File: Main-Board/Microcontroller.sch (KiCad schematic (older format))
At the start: 32 parts, among them J6 USB_B_Micro, J7 ICSP, SW1 Reset, U3 FT232RL, U4 ATmega328P-AU, U5 LM1117-5.0, Y1 16 MHz

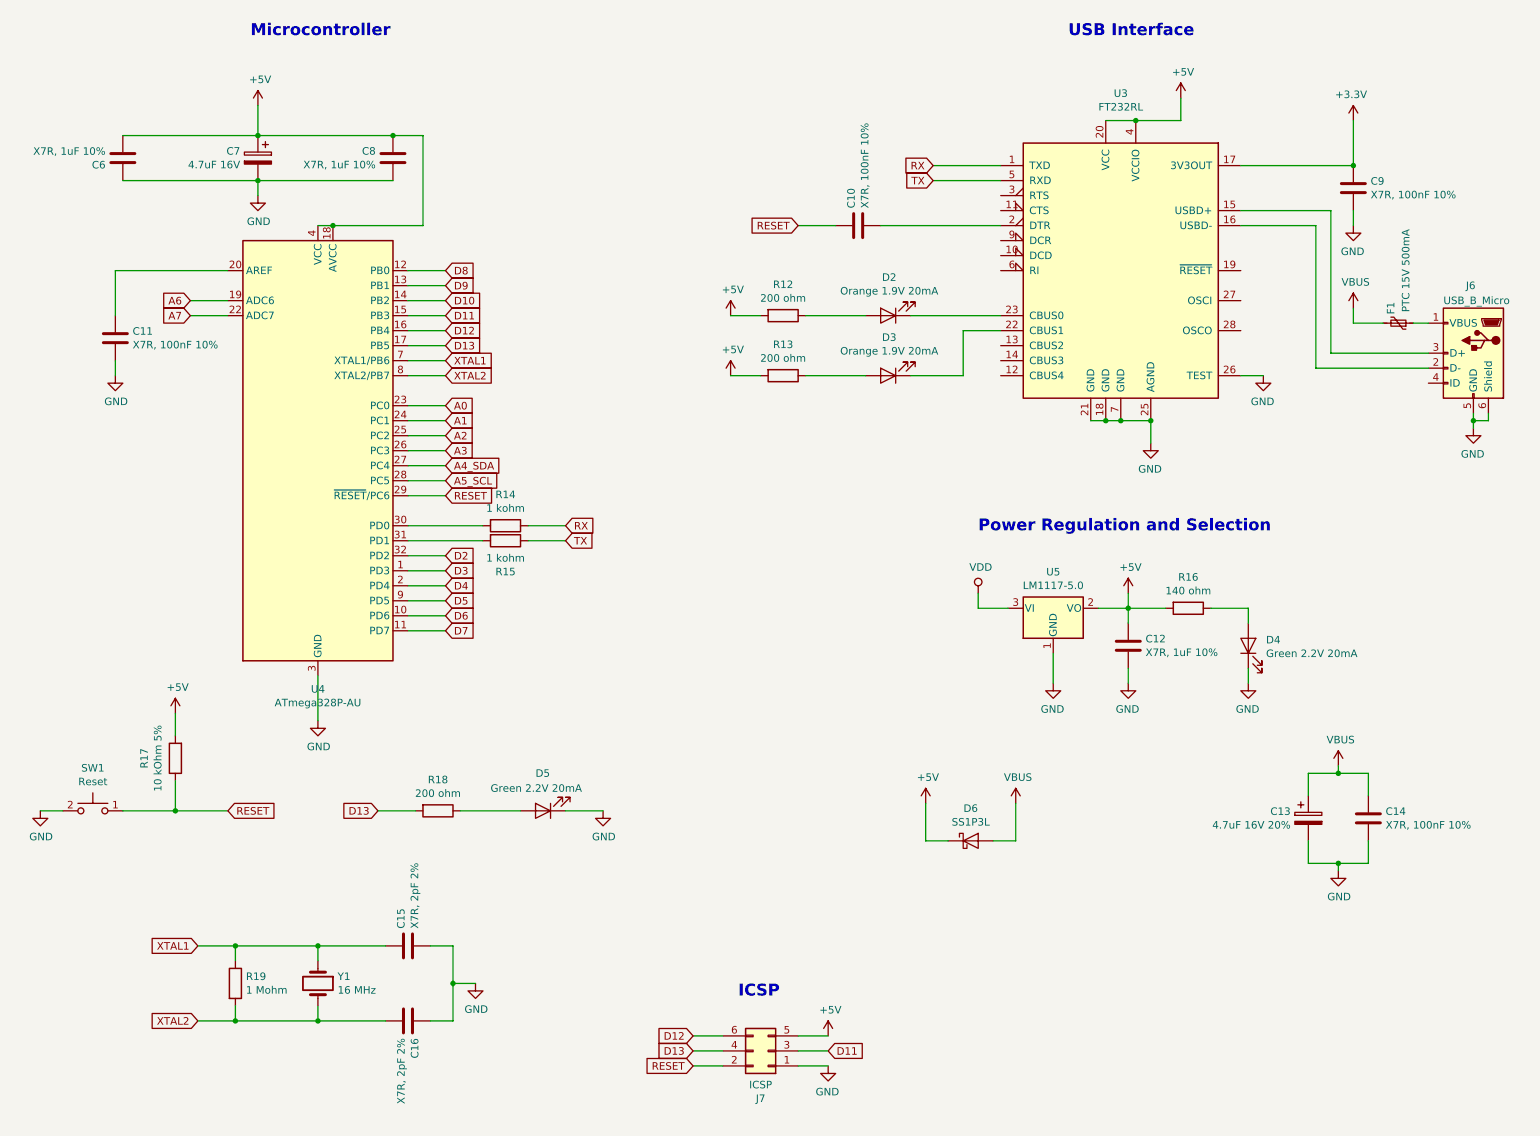
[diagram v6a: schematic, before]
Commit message: Review IMU, changed power in connector to 6 pos to prevent mis mating
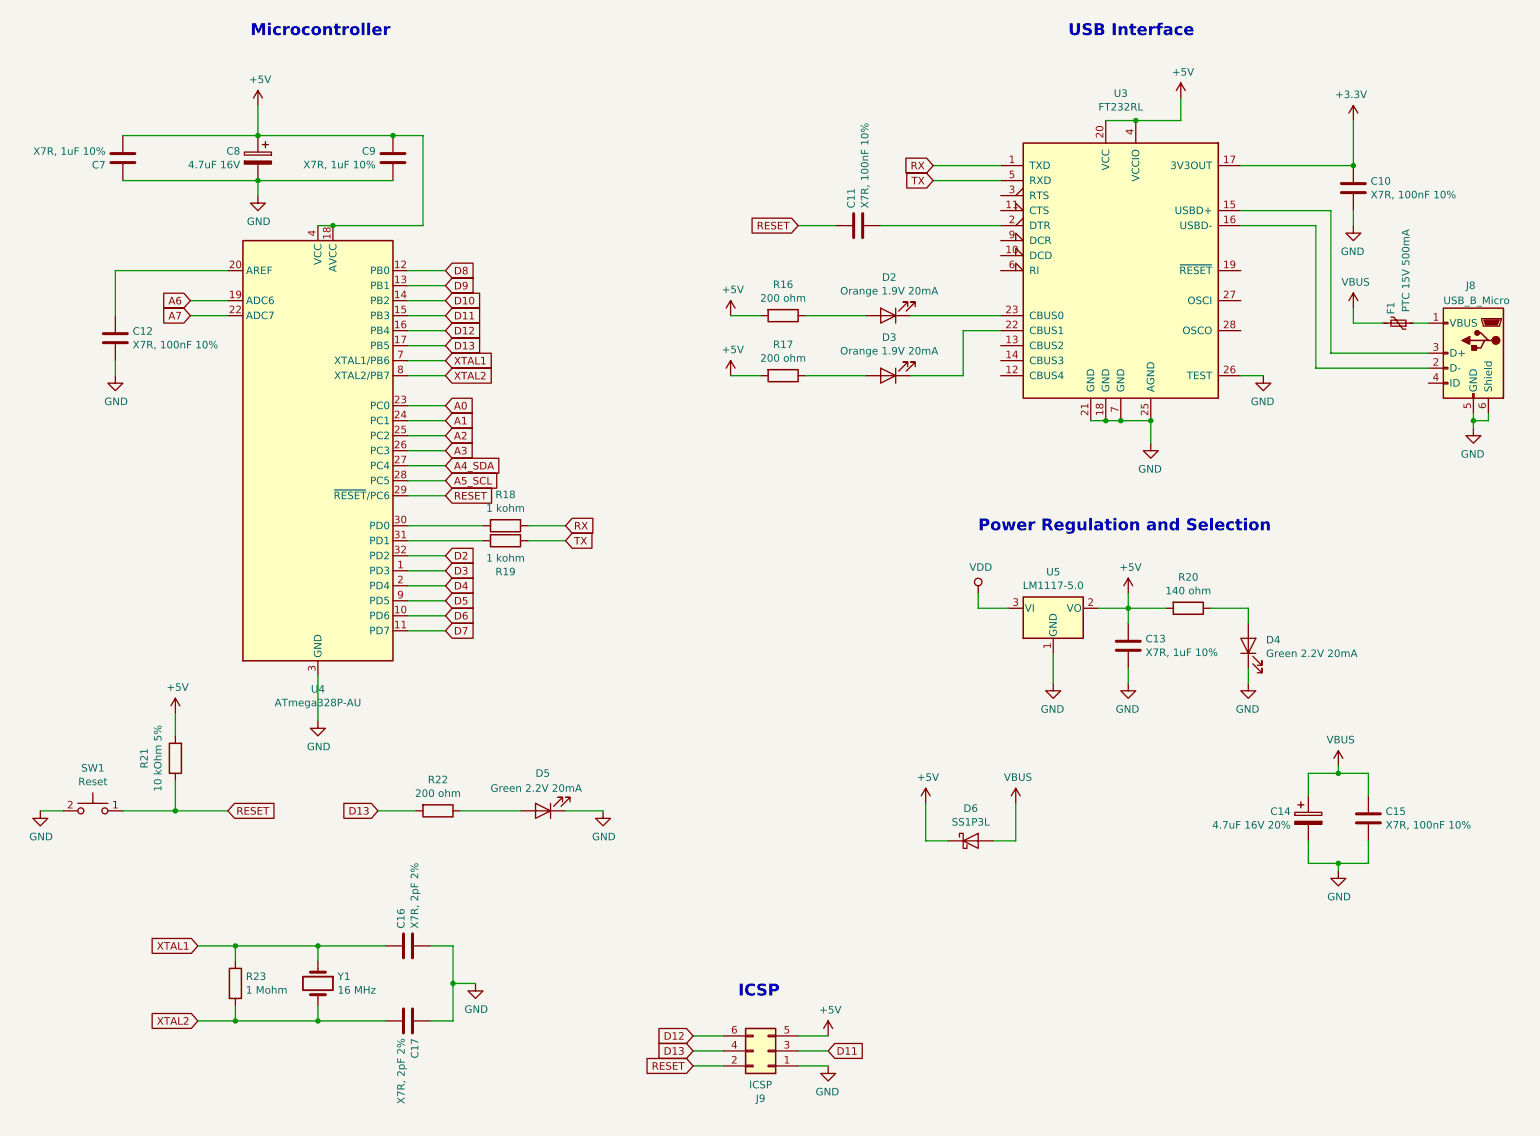
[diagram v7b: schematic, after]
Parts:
- renumbered C9 to C10, C10 to C11, C11 to C12, C12 to C13, C13 to C14, C14 to C15, C15 to C16, C16 to C17, C6 to C7, C7 to C8, C8 to C9, J6 to J8, J7 to J9, R12 to R16, R13 to R17, R14 to R18, R15 to R19, R16 to R20, R17 to R21, R18 to R22, R19 to R23

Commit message: Initial glance over microcontroller schematic
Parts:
- C10, C11, C15: value X7R, 100nF 10% -> 100nF 16V X7R 10%
- C13, C7, C9: value X7R, 1uF 10% -> 1uF 16V X7R 10%
- C16, C17: value X7R, 2pF 2% -> 2pF 16V X7R 2%
- R18, R19: value 1 kohm -> 1 kohm 5%
- R21: value 10 kOhm 5% -> 1 kohm 5%
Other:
- note added: "5V Regulation and Selection"
- note removed: "Power Regulation and Selection"
- moved on the sheet: C12, C13, C7, C8, C9, D4, D5, J9, R18, R19, R21, R22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
